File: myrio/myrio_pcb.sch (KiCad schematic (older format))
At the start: 126 parts, among them J1 CONN_02X03, J2 CONN_02X03, J3 CONN_02X03, J4 CONN_02X03, P1 CONN_02X17, P2 CONN_02X17, Q1 PN2222A, Q10 PN2222A, Q11 PN2222A, Q12 PN2222A, Q13 PN2222A, Q14 PN2222A, Q15 PN2222A, Q16 PN2222A, Q17 PN2222A, Q18 PN2222A, Q19 PN2222A, Q2 PN2222A, Q20 PN2222A, Q3 PN2222A, Q4 PN2222A, Q5 PN2222A, Q6 PN2222A, Q7 PN2222A, Q8 PN2222A, Q9 PN2222A, U1 stacked-DB9, U10 INA219, U11 INA219, U13 INA219, U14 stacked-rj45-LED, U15 stacked-rj45-LED, U2 stacked-DB9, U3 stacked-rj45-LED, U4 stacked-rj45-LED, U5 stacked-rj45-LED, U6 BNO055, U7 stacked-rj45-LED, U8 stacked-DB9

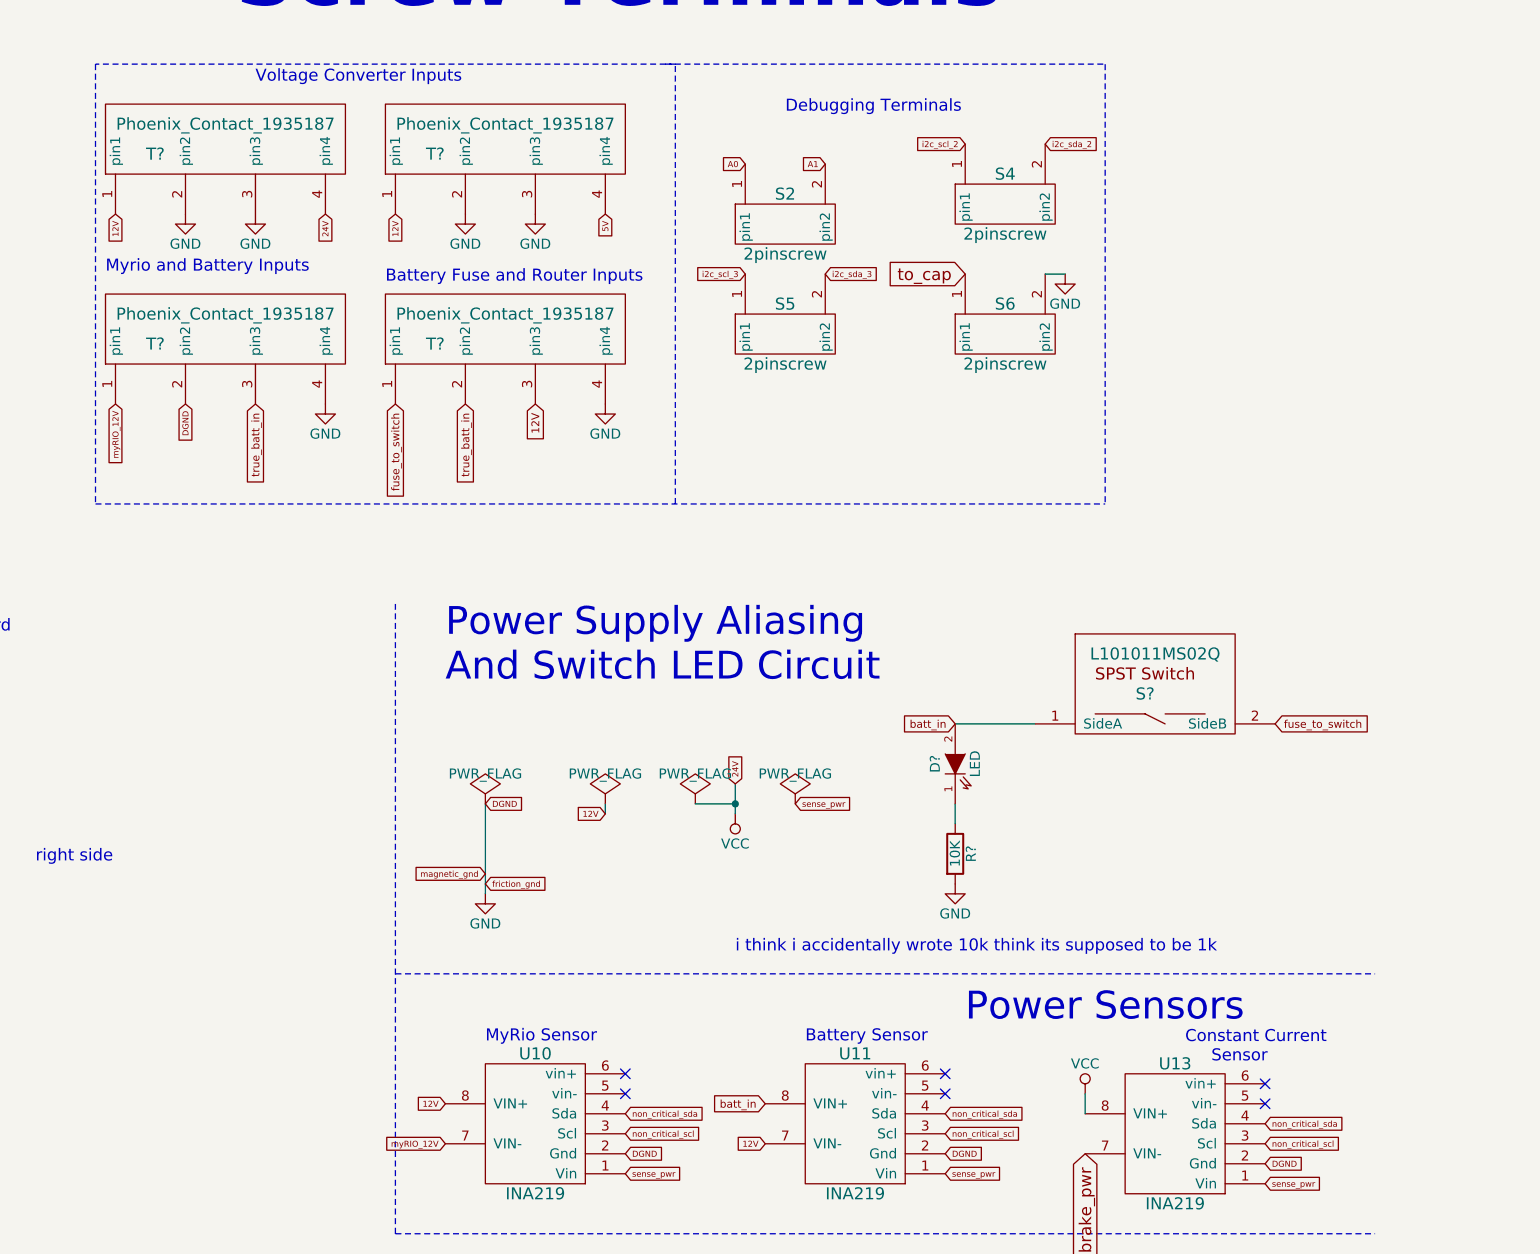
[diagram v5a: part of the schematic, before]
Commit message: renamed some stuff had to add some pwer flags so kicad would stop bitching. Dont worry though they do absolutly nothing to the circuit
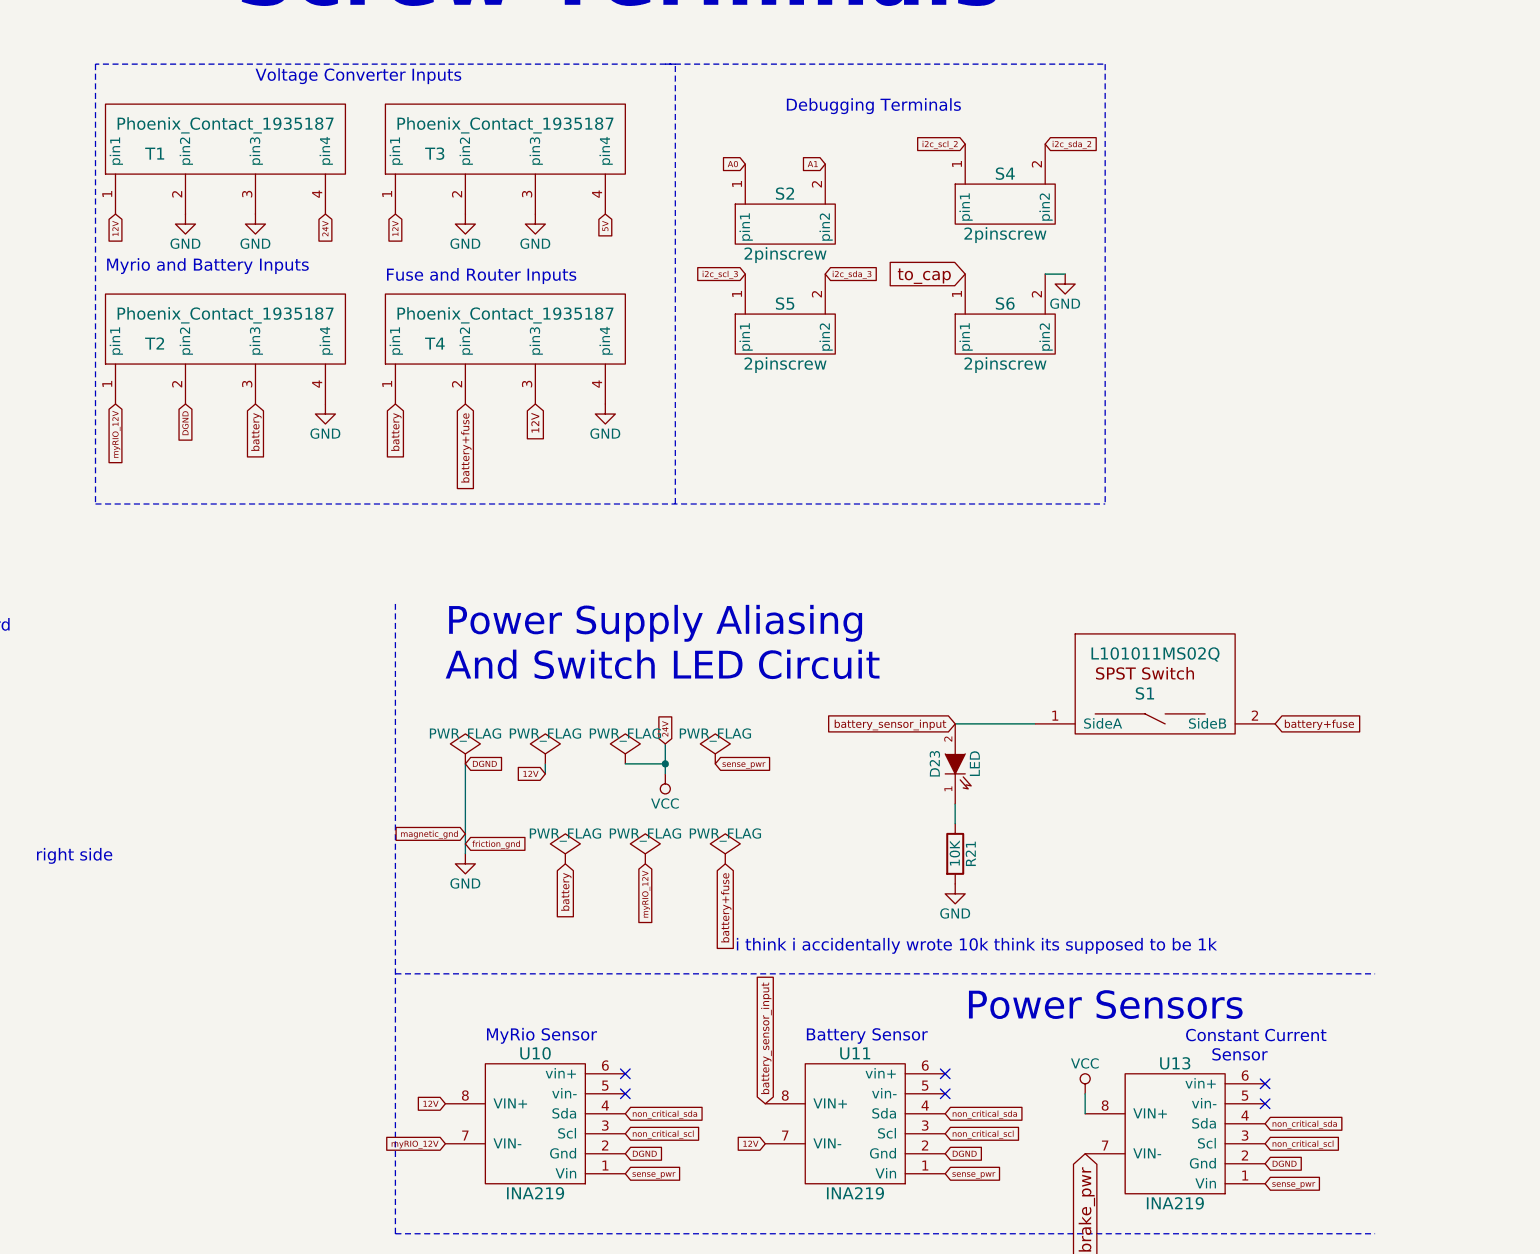
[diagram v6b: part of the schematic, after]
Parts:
- gave numbers to parts that had none: 7
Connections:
- net batt_in renamed battery_sensor_input
- net fuse_to_switch renamed battery
- net battery: now also T2.3 (pin3); no longer S1.2 (SideB)
- net true_batt_in renamed battery+fuse
- net battery+fuse: now also S1.2 (SideB); no longer T2.3 (pin3)
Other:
- note added: "Fuse and Router Inputs"
- note removed: "Battery Fuse and Router Inputs"

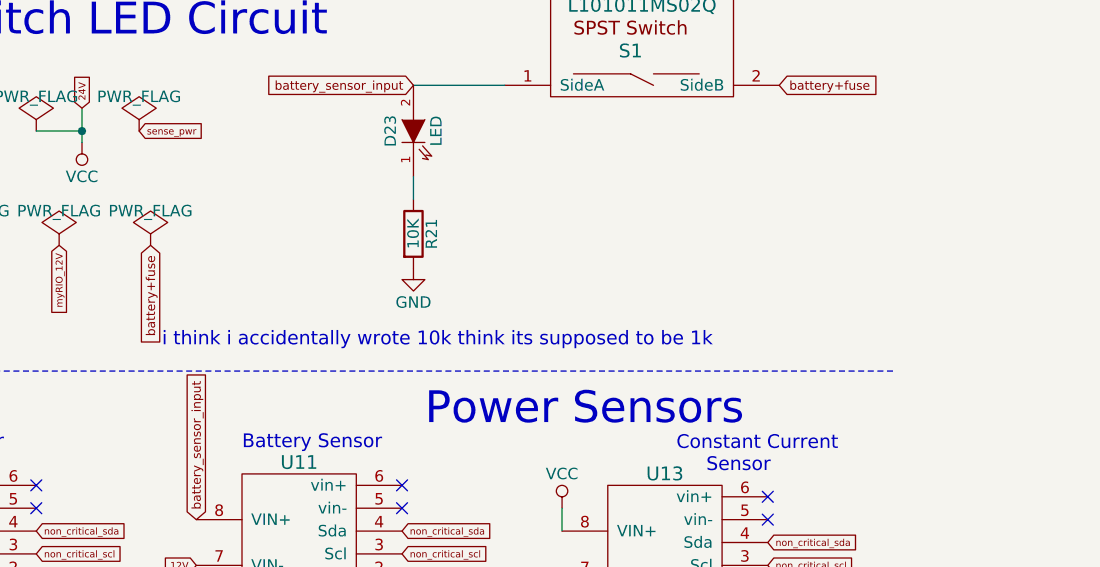
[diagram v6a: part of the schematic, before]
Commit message: fixed the resistor value
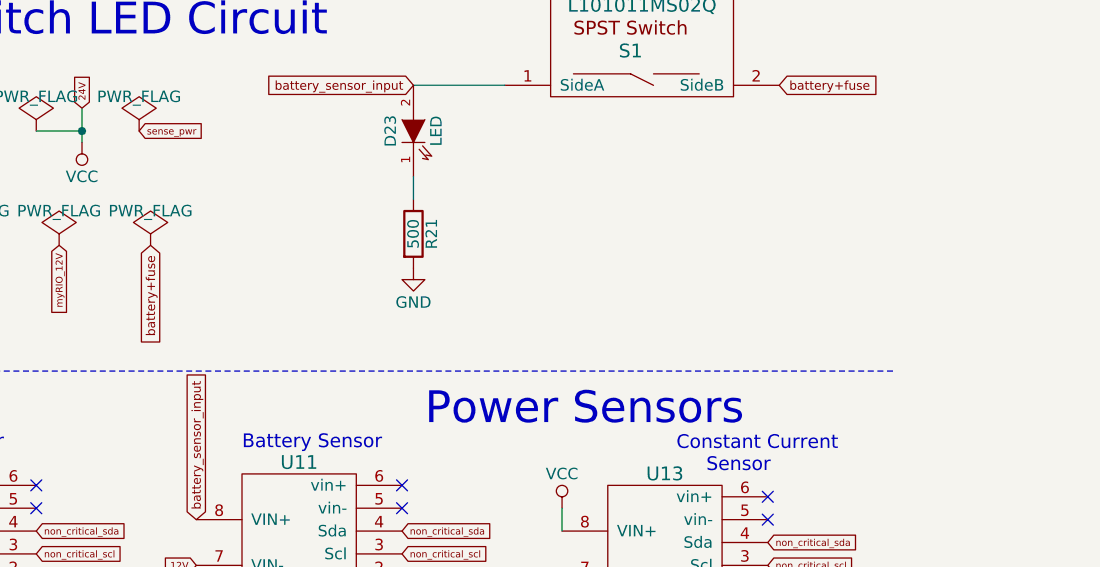
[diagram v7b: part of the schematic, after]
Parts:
- R21: value 10K -> 500
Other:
- note removed: "i think i accidentally wrote 10k think its supposed to be 1k"
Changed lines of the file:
@@
 P 9100 1750
 F 0 "R21" V 9180 1750 50  0000 C CNN
-F 1 "10K" V 9100 1750 50  0000 C CNN
+F 1 "500" V 9100 1750 50  0000 C CNN
 F 2 "" V 9030 1750 50  0000 C CNN
 F 3 "" H 9100 1750 50  0000 C CNN
@@
 Wire Wire Line
 	9100 1100 9500 1100
-Text Notes 8000 2250 0    60   ~ 0
-i think i accidentally wrote 10k think its supposed to be 1k
 Text GLabel 10700 1100 2    39   Input ~ 0
 battery+fuse

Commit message: layout done, still tracing
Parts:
- removed D21: ZENER, Discret:D3, symbol ZENER
- added R31: 12K, Resistors_THT:R_Axial_DIN0204_L3.6mm_D1.6mm_P5.08mm_Horizontal, symbol R
- added R32, R33: 2K, Resistors_THT:R_Axial_DIN0204_L3.6mm_D1.6mm_P5.08mm_Horizontal, symbol R
- D23: footprint (none) -> LEDs:LED_D5.0mm; symbol LED -> LED-RESCUE-myrio_pcb
- R21: footprint (none) -> Resistors_THT:R_Axial_DIN0204_L3.6mm_D1.6mm_P5.08mm_Horizontal
- R30: value R -> 12K
- S1: footprint (none) -> footprints:L101011MS02Q
- T1, T2, T3, T4: footprint (none) -> footprints:Phoenix_Contact_1935187
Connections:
- net labels added: laser_digital1, laser_digital2, main_laser1, main_laser2
- net labels removed: laser_digital, main_laser
- wire segments 204 -> 209
- no-connect marks 117 -> 113
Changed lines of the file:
@@
 EESchema Schematic File Version 2
 LIBS:myrio_pcb-rescue
+LIBS:power
+LIBS:device
+LIBS:transistors
+LIBS:conn
+LIBS:linear
+LIBS:regul
+LIBS:74xx
+LIBS:cmos4000
+LIBS:adc-dac
+LIBS:memory
+LIBS:xilinx
+LIBS:microcontrollers
+LIBS:dsp
+LIBS:microchip
+LIBS:analog_switches
+LIBS:motorola
+LIBS:texas
+LIBS:intel
+LIBS:audio
+LIBS:interface
+LIBS:digital-audio
+LIBS:philips
+LIBS:display
+LIBS:cypress
+LIBS:siliconi
+LIBS:opto
+LIBS:atmel
+LIBS:contrib
+LIBS:valves
 LIBS:relay
 LIBS:2pinscrew
@@
 pressure4-
 Text GLabel 3500 1650 2    30   Input ~ 0
-laser_digital
+laser_digital1
 Text GLabel 1850 4800 0    30   Input ~ 0
 friction_ctrl
@@
 	-1   0    0    1
 $EndComp
-Text GLabel 22050 950  2    60   Input ~ 0
+Text GLabel 22050 800  2    60   Input ~ 0
 to_cap
-NoConn ~ 22050 800
 Text GLabel 21100 650  0    30   Input ~ 0
 friction_pwr
@@
 DGND
 Text GLabel 5600 9850 0    30   Input ~ 0
-main_laser
+main_laser1
 NoConn ~ 5600 10150
 NoConn ~ 5600 10350
@@
 Text GLabel 8150 3000 1    39   Input ~ 0
 battery_sensor_input
-NoConn ~ 2600 1150
 NoConn ~ 2600 1250
 NoConn ~ 3100 950
@@
 Text GLabel 14600 3850 2    30   Input ~ 0
 24V
-NoConn ~ 5600 10250
 NoConn ~ 7450 2850
 NoConn ~ 7450 2950
@@
 DGND
 Text GLabel 10550 5350 0    30   Input ~ 0
-main_laser
+main_laser1
 $Comp
 L R R30
@@
 P 10650 5500
 F 0 "R30" V 10730 5500 50  0000 C CNN
-F 1 "R" V 10650 5500 50  0000 C CNN
+F 1 "12K" V 10650 5500 50  0000 C CNN
 F 2 "Resistors_THT:R_Axial_DIN0204_L3.6mm_D1.6mm_P5.08mm_Horizontal" V 10580 5500 50  0001 C CNN
 F 3 "" H 10650 5500 50  0000 C CNN
@@
 	1    0    0    -1
 $EndComp
-$Comp
-L ZENER D21
-U 1 1 58EA93BD
-P 10650 5950
-F 0 "D21" H 10650 6050 50  0000 C CNN
-F 1 "ZENER" H 10650 5850 50  0000 C CNN
-F 2 "Discret:D3" H 10650 5950 50  0001 C CNN
-F 3 "" H 10650 5950 50  0000 C CNN
-	1    10650 5950
-	0    1    1    0
-$EndComp
 Text GLabel 10750 5700 2    30   Input ~ 0
-laser_digital
+laser_digital1
 Text Notes 10100 5250 0    60   ~ 0
 Main Laser Circuit
@@
 Text GLabel 23700 900  2    30   Input ~ 0
 magnetic_pwr
-NoConn ~ 5600 9950
-NoConn ~ 5600 10050
 NoConn ~ 6700 10150
 NoConn ~ 6700 10350
@@
 NoConn ~ -250 11600
 $Comp
-L LED D23
+L LED-RESCUE-myrio_pcb D23
 U 1 1 596FFCA6
 P 9100 1300
 F 0 "D23" H 9100 1400 50  0000 C CNN
 F 1 "LED" H 9100 1200 50  0000 C CNN
-F 2 "" H 9100 1300 50  0000 C CNN
+F 2 "LEDs:LED_D5.0mm" H 9100 1300 50  0001 C CNN
 F 3 "" H 9100 1300 50  0000 C CNN
 	1    9100 1300
@@
 F 0 "R21" V 9180 1750 50  0000 C CNN
 F 1 "500" V 9100 1750 50  0000 C CNN
-F 2 "" V 9030 1750 50  0000 C CNN
+F 2 "Resistors_THT:R_Axial_DIN0204_L3.6mm_D1.6mm_P5.08mm_Horizontal" V 9030 1750 50  0001 C CNN
 F 3 "" H 9100 1750 50  0000 C CNN
 	1    9100 1750
@@
 F 0 "S1" H 10050 1050 60  0000 C CNN
 F 1 "L101011MS02Q" H 10100 1250 60  0000 C CNN
-F 2 "" H 10050 1000 60  0001 C CNN
+F 2 "footprints:L101011MS02Q" H 10050 1000 60  0001 C CNN
 F 3 "" H 10050 1000 60  0001 C CNN
 	1    10050 1000
@@
 F 0 "T1" H 5100 -1550 60  0000 C CNN
 F 1 "Phoenix_Contact_1935187" H 5450 -1400 60  0000 C CNN
-F 2 "" H 4900 -1650 60  0001 C CNN
+F 2 "footprints:Phoenix_Contact_1935187" H 4900 -1650 60  0001 C CNN
 F 3 "" H 4900 -1650 60  0001 C CNN
 	1    4900 -1650
@@
 F 0 "T3" H 6500 -1550 60  0000 C CNN
 F 1 "Phoenix_Contact_1935187" H 6850 -1400 60  0000 C CNN
-F 2 "" H 6300 -1650 60  0001 C CNN
+F 2 "footprints:Phoenix_Contact_1935187" H 6300 -1650 60  0001 C CNN
 F 3 "" H 6300 -1650 60  0001 C CNN
 	1    6300 -1650
@@
 F 0 "T2" H 5100 -600 60  0000 C CNN
 F 1 "Phoenix_Contact_1935187" H 5450 -450 60  0000 C CNN
-F 2 "" H 4900 -700 60  0001 C CNN
+F 2 "footprints:Phoenix_Contact_1935187" H 4900 -700 60  0001 C CNN
 F 3 "" H 4900 -700 60  0001 C CNN
 	1    4900 -700
@@
 F 0 "T4" H 6500 -600 60  0000 C CNN
 F 1 "Phoenix_Contact_1935187" H 6850 -450 60  0000 C CNN
-F 2 "" H 6300 -700 60  0001 C CNN
+F 2 "footprints:Phoenix_Contact_1935187" H 6300 -700 60  0001 C CNN
 F 3 "" H 6300 -700 60  0001 C CNN
 	1    6300 -700
@@
 Text GLabel 7150 1800 3    39   Input ~ 0
 battery
+$Comp
+L R R33
+U 1 1 59787DC0
+P 10650 5900
+F 0 "R33" V 10730 5900 50  0000 C CNN
+F 1 "2K" V 10650 5900 50  0000 C CNN
+F 2 "Resistors_THT:R_Axial_DIN0204_L3.6mm_D1.6mm_P5.08mm_Horizontal" V 10580 5900 50  0001 C CNN
+F 3 "" H 10650 5900 50  0000 C CNN
+	1    10650 5900
+	1    0    0    -1
+$EndComp
+Wire Wire Line
+	10650 6050 10650 6150
+Text GLabel 10100 6150 3    30   Input ~ 0
+DGND
+Text GLabel 10000 5350 0    30   Input ~ 0
+main_laser2
+$Comp
+L R R31
+U 1 1 59789155
+P 10100 5500
+F 0 "R31" V 10180 5500 50  0000 C CNN
+F 1 "12K" V 10100 5500 50  0000 C CNN
+F 2 "Resistors_THT:R_Axial_DIN0204_L3.6mm_D1.6mm_P5.08mm_Horizontal" V 10030 5500 50  0001 C CNN
+F 3 "" H 10100 5500 50  0000 C CNN
+	1    10100 5500
+	1    0    0    -1
+$EndComp
+Text GLabel 10200 5700 2    30   Input ~ 0
+laser_digital2
+Wire Wire Line
+	10100 5650 10100 5750
+Wire Wire Line
+	10100 5700 10200 5700
+Connection ~ 10100 5700
+Wire Wire Line
+	10000 5350 10100 5350
+$Comp
+L R R32
+U 1 1 59789160
+P 10100 5900
+F 0 "R32" V 10180 5900 50  0000 C CNN
+F 1 "2K" V 10100 5900 50  0000 C CNN
+F 2 "Resistors_THT:R_Axial_DIN0204_L3.6mm_D1.6mm_P5.08mm_Horizontal" V 10030 5900 50  0001 C CNN
+F 3 "" H 10100 5900 50  0000 C CNN
+	1    10100 5900
+	1    0    0    -1
+$EndComp
+Wire Wire Line
+	10100 6050 10100 6150
+Text GLabel 2600 1150 0    30   Input ~ 0
+laser_digital2
+Text GLabel 5600 9950 0    30   Input ~ 0
+24V
+Text GLabel 5600 10050 0    30   Input ~ 0
+DGND
+Text GLabel 5600 10250 0    30   Input ~ 0
+main_laser2
+NoConn ~ 22050 950
 $EndSCHEMATC
